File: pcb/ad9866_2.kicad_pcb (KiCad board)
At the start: 4 copper layers, 50 x 50 mm, 105 parts, among them CN1 MEC6-140_CONNECTOR_BEMICRO, CON1 USB-MICRO-B, P1 CONN_2, P10 CONN_1, P2 CONN_10X2, P3 CONN_1, P4 CONN_5X2, P5 CONN_1, P5V0 CONN_1, P6 Coaxial_Connector, P7 Coaxial_Connector, P8 CONN_2, P9 CONN_1, Q1 Si2301, T1 TRANSF_ADT2, T2 TRANSF_ADT8, U1 NCP1117ST33T3G, U2 NCP1117ST33T3G, U3 Si510, U4 AD9866BCPZ, U5 NCP1117ST33T3G, U6 25AA02E48T-I/OT

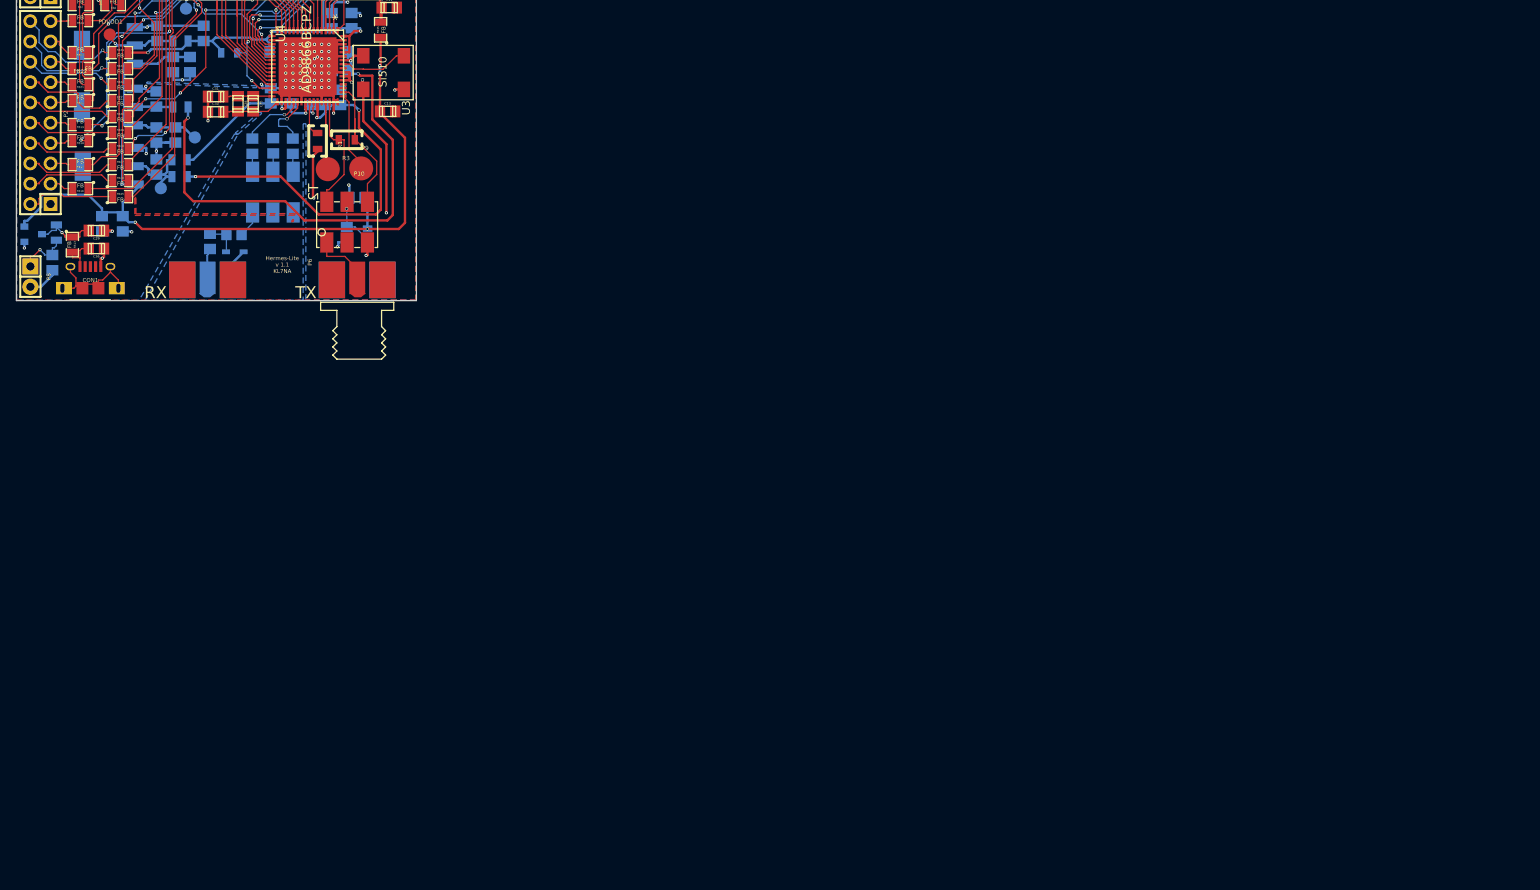
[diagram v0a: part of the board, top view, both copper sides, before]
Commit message: Fixed the ADC reference caps.
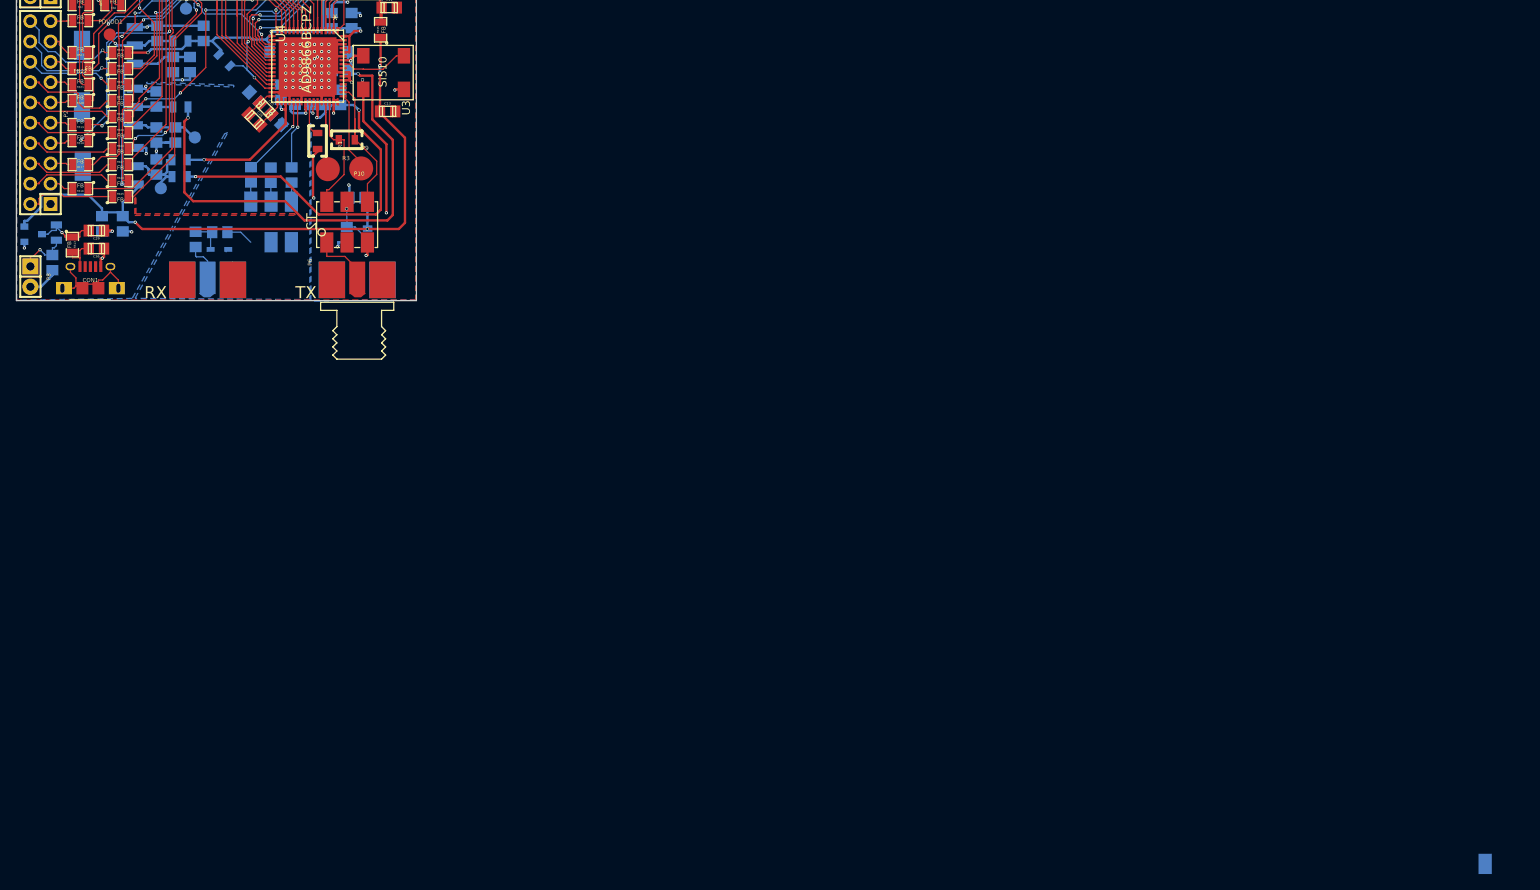
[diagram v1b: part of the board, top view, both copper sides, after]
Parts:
- C30, C31: moved to B.Cu
- moved C30 7.63 mm to (157.5, 62.3), turned to 135 degrees
- moved C31 4.90 mm to (154.8, 59.6), turned to 315 degrees
- moved T2 3.73 mm to (159.4, 79.0)
- moved C17 3.69 mm to (156.8, 69.3)
- moved C19 3.60 mm to (159.4, 69.3)
- moved C18 3.58 mm to (154.3, 69.3)
- moved C28 2.85 mm to (154.8, 62.4), turned to 315 degrees
- moved D1 1.95 mm to (150.4, 78.6)
- moved C35 1.82 mm to (147.4, 77.3)
- moved C32 1.79 mm to (150.4, 76.5)
- moved C25 1.65 mm to (156.2, 61.0), turned to 315 degrees
- moved C16 1.33 mm to (158.1, 59.0)
- moved R2 1.10 mm to (151.0, 55.0), turned to 315 degrees
- moved C15 0.55 mm to (159.8, 59.6)
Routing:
- net GND: track 152.3 -> 145.2 mm, vias 84 -> 82
- net Net-(C25-Pad1): track 7.99 -> 3.87 mm, vias 0 -> 1
- net Net-(C35-Pad2): track 9.67 -> 7.20 mm
- net /AVDD_ADC: track 22.6 -> 24.9 mm, vias 2 -> 3
- net Net-(C25-Pad2): track 6.13 -> 3.83 mm, vias 0 -> 1
- net /RXN: track 8.99 -> 11.3 mm
- net Net-(CN1-Pad31): track 17.5 -> 19.5 mm
- net /RXP: track 8.37 -> 9.47 mm
- net Net-(C32-Pad2): track 4.29 -> 4.93 mm

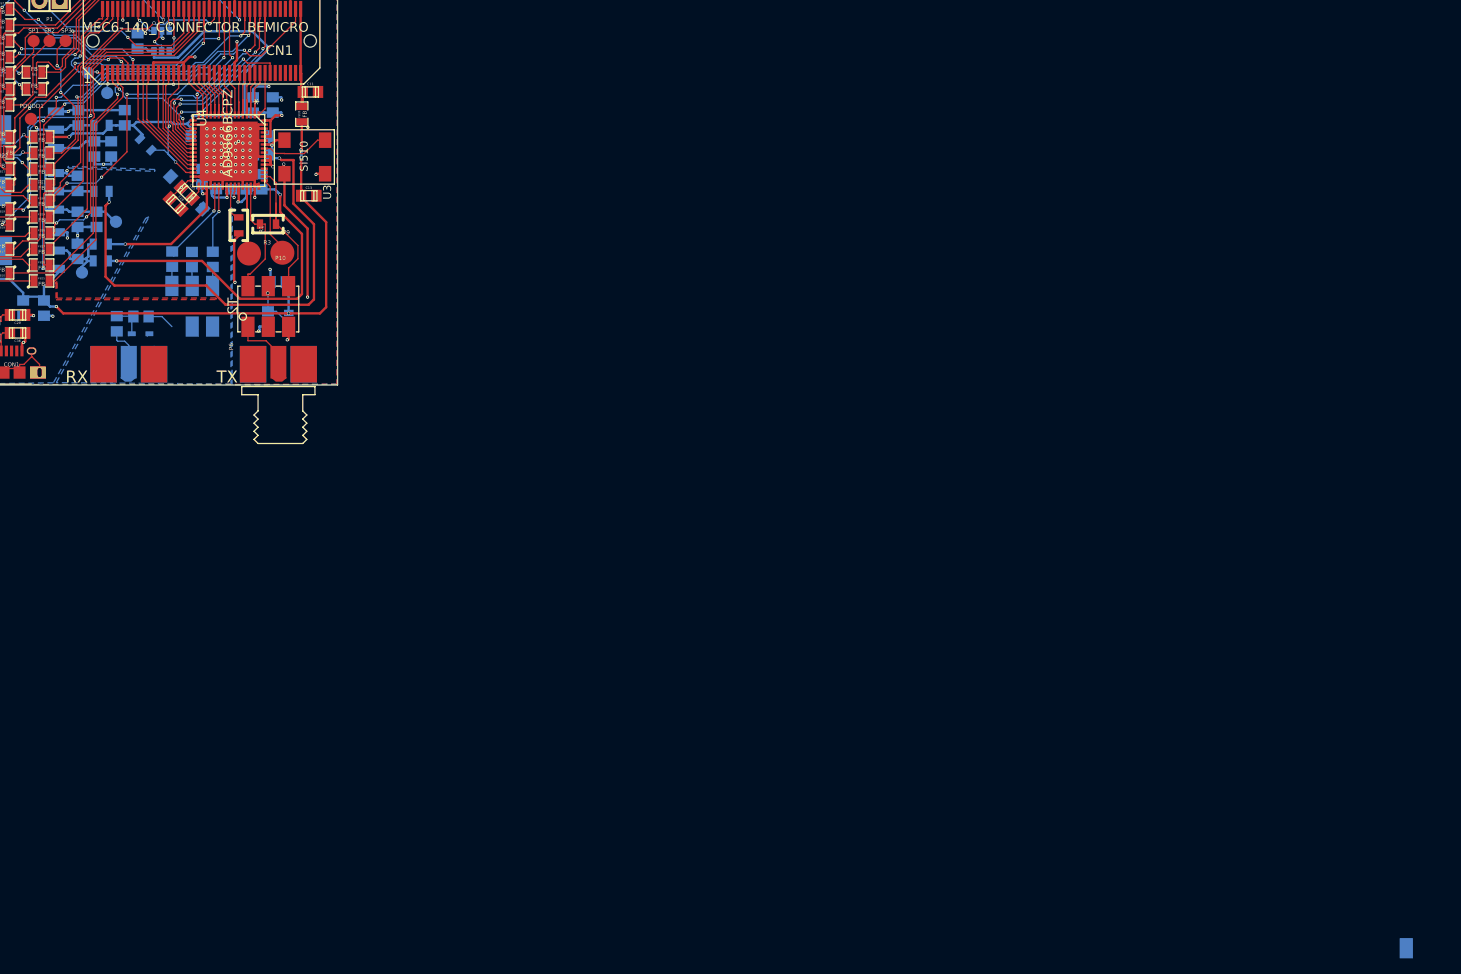
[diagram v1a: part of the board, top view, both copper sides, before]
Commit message: Added more FB's and bypass caps.
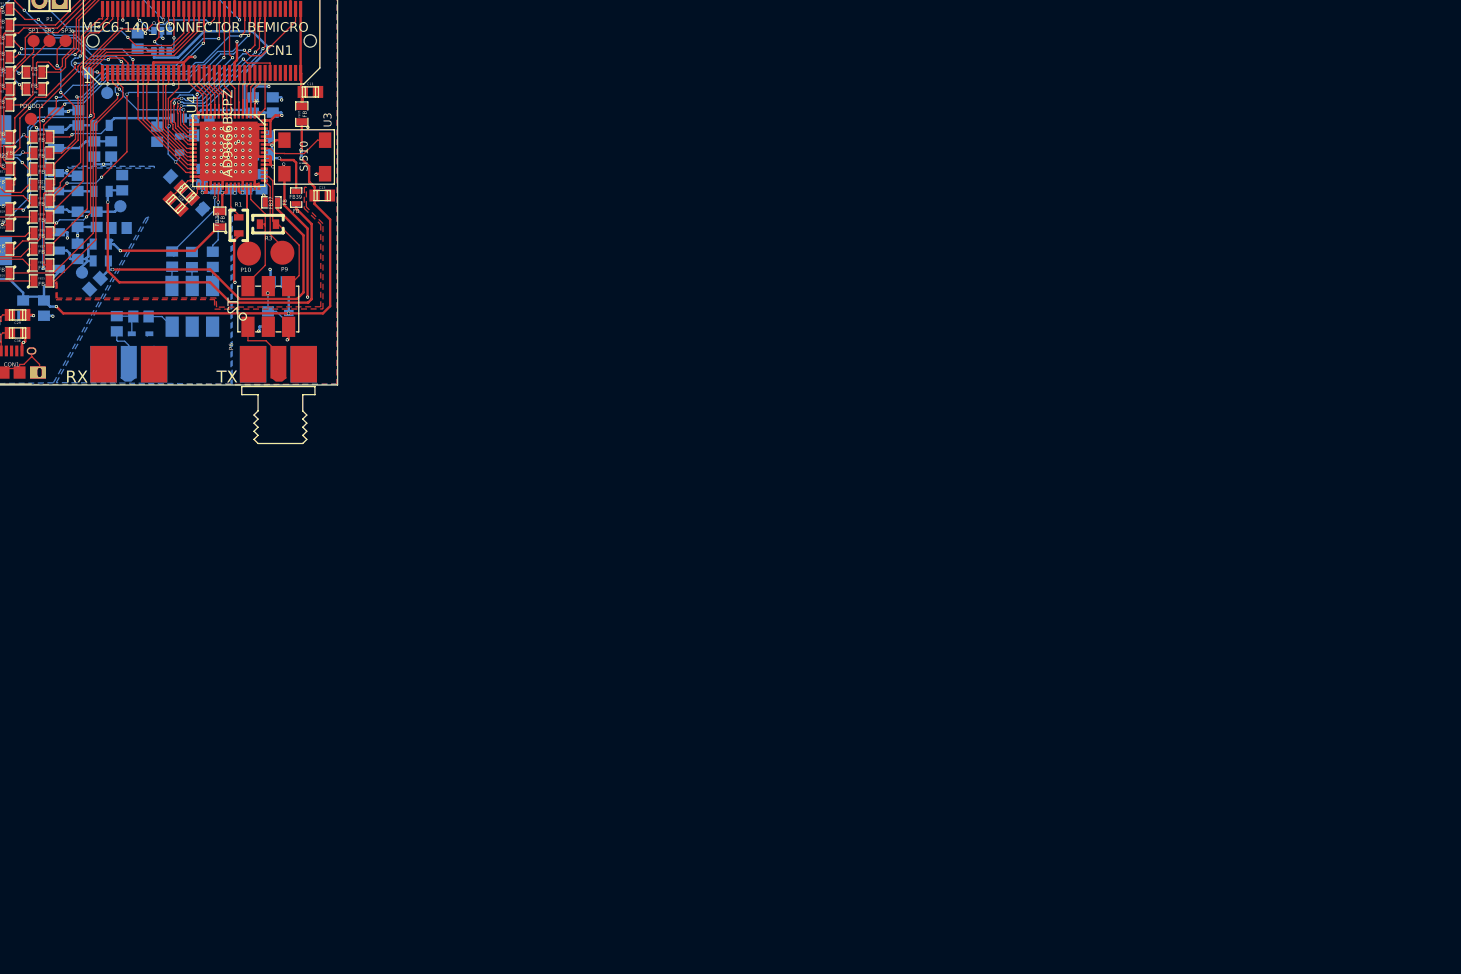
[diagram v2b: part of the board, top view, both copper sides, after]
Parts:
- added C22: 0.1UF, Capacitors_SMD:c_0805, B.Cu at (147.7, 65.4)
- added C26: 0.1UF, Capacitors_SMD:c_0805, B.Cu at (144.7, 72.4)
- added C40: 0.1UF, Capacitors_SMD:c_0805, B.Cu at (152.4, 53.6)
- added C41: 0.1UF, Capacitors_SMD:c_0805, B.Cu at (148.1, 59.7)
- added FB36: FB, SMD_Packages:SM0805, F.Cu at (160.3, 64.3)
- added FB37: FB, SMD_Packages:SM0603_Resistor, F.Cu at (166.7, 62.2)
- added FB38: FB, SMD_Packages:SM0603_Resistor, B.Cu at (155.1, 51.6)
- added FB39: FB, SMD_Packages:SM0603_Resistor, F.Cu at (169.8, 61.6)
- moved C10 9.87 mm to (158.0, 53.8), turned to 180 degrees
- moved R2 4.25 mm to (155.2, 55.0), turned to 270 degrees
- moved C8 2.04 mm to (158.0, 51.9)
- moved P5V0 2.02 mm to (147.8, 62.7)
- moved C13 1.68 mm to (173.1, 61.3)
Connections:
- FB10 pad 2: /AVDD_ADC -> Net-(C22-Pad1)
- FB11 pad 2: /AVDD_DAC -> Net-(C26-Pad1)
- FB12 pad 2: /DVDD -> /EX_3V3
- FB14 pad 2: /CLKVDD -> Net-(C41-Pad1)
- FB34 pad 2: /DVDD -> /EX_3V3
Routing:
- net /CLKVDD: track 67.9 -> 14.8 mm, vias 3 -> 2
- net Net-(C41-Pad1): track 0.00 -> 51.9 mm, vias 0 -> 1
- net Net-(C26-Pad1): track 0.00 -> 44.0 mm, vias 0 -> 1
- net /AVDD_DAC: track 49.9 -> 6.08 mm, vias 3 -> 2
- net Net-(C22-Pad1): track 0.00 -> 19.4 mm, vias 0 -> 1
- net /EX_3V3: track 0.00 -> 17.9 mm, vias 0 -> 1
- net /DVDD: track 69.5 -> 52.5 mm, vias 3 -> 2
- net /AVDD_ADC: track 24.9 -> 9.69 mm, vias 3 -> 2
- net GND: track 145.2 -> 138.0 mm, vias 82 -> 81
- net Net-(CN1-Pad31): track 19.5 -> 17.3 mm
- net Net-(R3-Pad1): track 18.9 -> 16.9 mm
- net Net-(C24-Pad1): track 2.77 -> 1.50 mm
- net Net-(CN1-Pad5): track 14.9 -> 15.5 mm
